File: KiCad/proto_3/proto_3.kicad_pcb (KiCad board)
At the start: 2 copper layers, 129 x 49 mm, 13 parts, among them J1 1729128, J2 1729128

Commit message: removed AC markings on L and N lines on AC input. Added individual L and P symbols to AC input lines. Need to create nets for each.
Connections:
- net Net-(D1-A1) renamed +5V
- C2 pad 2: Net-(D1-A2) -> GND
- C3 pad 2: Net-(D1-A2) -> GND
- C4 pad 2: Net-(D1-A2) -> GND
- CY1 pad 2: Net-(D1-A2) -> GND
- D1 pad 2: Net-(D1-A2) -> GND
- FUSE1 pad 1: Net-(FUSE1-Pad1) -> AC
- J1 pad 2: Net-(D1-A2) -> GND
- J2 pad 1: GND -> AC
- J2 pad 2: Net-(FUSE1-Pad1) -> AC
- U1 pad 2: GND -> AC
- U1 pad 5: Net-(D1-A2) -> GND
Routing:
- net AC: track 0.00 -> 141.5 mm
- net Net-(D1-A2): track 106.1 -> 0.00 mm
- net Net-(FUSE1-Pad1): track 40.0 -> 0.00 mm
- net GND: track 101.6 -> 106.1 mm
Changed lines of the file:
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@@
 	(net 6 "Net-(LDM1-Pad2)")
 	(net 7 "GND")
-	(net 8 "Net-(D1-A2)")
-	(net 9 "Net-(D1-A1)")
-	(net 10 "Net-(FUSE1-Pad1)")
+	(net 8 "+5V")
+	(net 9 "AC")
 	(footprint "Capacitor-470uF-16V:CAP_RHT_8X11P5_NCH"
 		(layer "F.Cu")
@@
 			(layers "*.Cu" "*.Mask")
 			(remove_unused_layers no)
-			(net 8 "Net-(D1-A2)")
+			(net 7 "GND")
 			(pintype "unspecified")
 		)
@@
 			(layers "*.Cu" "*.Mask")
 			(remove_unused_layers no)
-			(net 9 "Net-(D1-A1)")
+			(net 8 "+5V")
 			(pinfunction "1")
 			(pintype "unspecified")
@@
 			(layers "*.Cu" "*.Mask")
 			(remove_unused_layers no)
-			(net 7 "GND")
+			(net 9 "AC")
 			(pinfunction "AC(N)")
 			(pintype "bidirectional")
@@
 			(layers "*.Cu" "*.Mask")
 			(remove_unused_layers no)
-			(net 8 "Net-(D1-A2)")
+			(net 7 "GND")
 			(pinfunction "-Vo")
 			(pintype "bidirectional")
@@
 		)
 		(property "Datasheet" "1729128"
-			(at 0 0 90)
+			(at 0 0 270)
 			(layer "F.Fab")
 			(hide yes)
@@
 		)
 		(property "Description" ""
-			(at 0 0 90)
+			(at 0 0 270)
 			(layer "F.Fab")
 			(hide yes)
@@
 			(layers "*.Cu" "*.Mask")
 			(remove_unused_layers no)
-			(net 9 "Net-(D1-A1)")
+			(net 8 "+5V")
 			(pinfunction "1")
 			(pintype "unspecified")
@@
 			(layers "*.Cu" "*.Mask")
 			(remove_unused_layers no)
-			(net 8 "Net-(D1-A2)")
+			(net 7 "GND")
 			(pinfunction "2")
 			(pintype "unspecified")
@@
 			(layers "*.Cu" "*.Mask")
 			(remove_unused_layers no)
-			(net 9 "Net-(D1-A1)")
+			(net 8 "+5V")
 			(pintype "unspecified")
 		)
@@
 			(layers "*.Cu" "*.Mask")
 			(remove_unused_layers no)
-			(net 8 "Net-(D1-A2)")
+			(net 7 "GND")
 			(pintype "unspecified")
 		)
@@
 		(embedded_fonts no)
 		(model "/home/none/Downloads/AIUR_06_472K/AIUR-06_ABR.step"
-			(hide yes)
 			(offset
 				(xyz 0 0 0)
@@
 			(size 2.1844 2.1844)
 			(layers "F.Cu" "F.Mask" "F.Paste")
-			(net 9 "Net-(D1-A1)")
+			(net 8 "+5V")
 			(pinfunction "A1")
 			(pintype "passive")
@@
 			(size 2.1844 2.1844)
 			(layers "F.Cu" "F.Mask" "F.Paste")
-			(net 8 "Net-(D1-A2)")
+			(net 7 "GND")
 			(pinfunction "A2")
 			(pintype "passive")
@@
 			(layers "*.Cu" "*.Mask")
 			(remove_unused_layers no)
-			(net 8 "Net-(D1-A2)")
+			(net 7 "GND")
 			(pintype "passive")
 			(solder_mask_margin 0.102)
@@
 			(layers "*.Cu" "*.Mask")
 			(remove_unused_layers no)
-			(net 10 "Net-(FUSE1-Pad1)")
+			(net 9 "AC")
 			(pinfunction "1")
 			(pintype "unspecified")
@@
 			(layers "*.Cu" "*.Mask")
 			(remove_unused_layers no)
-			(net 9 "Net-(D1-A1)")
+			(net 8 "+5V")
 			(pintype "unspecified")
 		)
@@
 			(layers "*.Cu" "*.Mask")
 			(remove_unused_layers no)
-			(net 8 "Net-(D1-A2)")
+			(net 7 "GND")
 			(pintype "unspecified")
 		)
@@
 		)
 		(property "Datasheet" "1729128"
-			(at 0 0 90)
+			(at 0 0 270)
 			(layer "F.Fab")
 			(hide yes)
@@
 		)
 		(property "Description" ""
-			(at 0 0 90)
+			(at 0 0 270)
 			(layer "F.Fab")
 			(hide yes)
@@
 			(layers "*.Cu" "*.Mask")
 			(remove_unused_layers no)
-			(net 7 "GND")
+			(net 9 "AC")
 			(pinfunction "1")
 			(pintype "unspecified")
@@
 			(layers "*.Cu" "*.Mask")
 			(remove_unused_layers no)
-			(net 10 "Net-(FUSE1-Pad1)")
+			(net 9 "AC")
 			(pinfunction "2")
 			(pintype "unspecified")
@@
 	)
 	(segment
-		(start 116.5 118.62)
-		(end 202.5 118.62)
-		(width 0.7814)
-		(layer "F.Cu")
-		(net 7)
-	)
-	(segment
-		(start 202.5 118.62)
-		(end 212.7 118.62)
-		(width 0.7814)
-		(layer "F.Cu")
-		(net 7)
-	)
-	(segment
-		(start 212.7 118.62)
-		(end 216.5 122.42)
-		(width 0.7814)
-		(layer "F.Cu")
-		(net 7)
-	)
-	(segment
 		(start 192.5 107.12)
 		(end 206.5 107.12)
 		(width 0.7814)
 		(layer "F.Cu")
-		(net 8)
+		(net 7)
 	)
 	(segment
@@
 		(width 0.7814)
 		(layer "F.Cu")
-		(net 8)
+		(net 7)
 	)
 	(segment
@@
 		(width 0.7814)
 		(layer "F.Cu")
-		(net 8)
+		(net 7)
 	)
 	(segment
@@
 		(width 0.7814)
 		(layer "F.Cu")
-		(net 8)
+		(net 7)
 	)
 	(segment
@@
 		(width 0.7814)
 		(layer "F.Cu")
-		(net 8)
+		(net 7)
 	)
 	(segment
@@
 		(width 0.7814)
 		(layer "F.Cu")
-		(net 8)
+		(net 7)
 	)
 	(segment
@@
 		(width 0.7814)
 		(layer "F.Cu")
-		(net 8)
+		(net 7)
 	)
 	(segment
@@
 		(width 0.7814)
 		(layer "F.Cu")
-		(net 8)
+		(net 7)
 	)
 	(segment
@@
 		(width 0.7814)
 		(layer "F.Cu")
-		(net 8)
+		(net 7)
 	)
 	(segment
@@
 		(width 0.7814)
 		(layer "F.Cu")
-		(net 8)
+		(net 7)
 	)
 	(segment
@@
 		(width 0.7814)
 		(layer "F.Cu")
-		(net 8)
+		(net 7)
 	)
 	(segment
@@
 		(width 0.7814)
 		(layer "F.Cu")
-		(net 8)
+		(net 7)
 	)
 	(segment
@@
 		(width 0.7814)
 		(layer "F.Cu")
-		(net 8)
+		(net 7)
 	)
 	(segment
@@
 		(width 0.7814)
 		(layer "F.Cu")
-		(net 8)
+		(net 7)
 	)
 	(segment
@@
 		(width 0.7814)
 		(layer "F.Cu")
-		(net 8)
+		(net 7)
 	)
 	(segment
@@
 		(width 0.7814)
 		(layer "F.Cu")
-		(net 8)
+		(net 7)
 	)
 	(segment
@@
 		(width 0.7814)
 		(layer "F.Cu")
-		(net 8)
+		(net 7)
 	)
 	(segment
@@
 		(width 0.7814)
 		(layer "F.Cu")
-		(net 9)
+		(net 8)
 	)
 	(segment
@@
 		(width 0.7814)
 		(layer "F.Cu")
-		(net 9)
+		(net 8)
 	)
 	(segment
@@
 		(width 0.7814)
 		(layer "F.Cu")
-		(net 9)
+		(net 8)
 	)
 	(segment
@@
 		(width 0.2)
 		(layer "F.Cu")
-		(net 9)
+		(net 8)
 	)
 	(segment
@@
 		(width 0.2)
 		(layer "F.Cu")
-		(net 9)
+		(net 8)
 	)
 	(segment
@@
 		(width 0.7814)
 		(layer "F.Cu")
-		(net 9)
+		(net 8)
 	)
 	(segment
@@
 		(width 0.7814)
 		(layer "F.Cu")
-		(net 9)
+		(net 8)
 	)
 	(segment
@@
 		(width 0.2)
 		(layer "F.Cu")
-		(net 9)
+		(net 8)
 	)
 	(segment
@@
 		(width 0.7814)
 		(layer "F.Cu")
-		(net 9)
+		(net 8)
 	)
 	(segment
@@
 		(width 0.7814)
 		(layer "F.Cu")
-		(net 9)
+		(net 8)
 	)
 	(segment
@@
 		(width 0.7814)
 		(layer "F.Cu")
+		(net 8)
+	)
+	(segment
+		(start 116.5 118.62)
+		(end 202.5 118.62)
+		(width 0.7814)
+		(layer "F.Cu")
 		(net 9)
 	)
@@
 		(width 0.7814)
 		(layer "F.Cu")
-		(net 10)
+		(net 9)
+	)
+	(segment
+		(start 202.5 118.62)
+		(end 212.7 118.62)
+		(width 0.7814)
+		(layer "F.Cu")
+		(net 9)
+	)
+	(segment
+		(start 212.7 118.62)
+		(end 216.5 122.42)
+		(width 0.7814)
+		(layer "F.Cu")
+		(net 9)
 	)
 	(segment
@@
 		(width 0.7814)
 		(layer "F.Cu")
-		(net 10)
+		(net 9)
 	)
 	(segment
@@
 		(width 0.7814)
 		(layer "F.Cu")
-		(net 10)
+		(net 9)
 	)
 	(zone

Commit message: labeled nets and netclasses for organization
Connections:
- FUSE1 pad 1: AC -> Net-(FUSE1-Pad1)
- J2 pad 1: AC -> Net-(U1-AC(N))
- J2 pad 2: AC -> Net-(FUSE1-Pad1)
- U1 pad 2: AC -> Net-(U1-AC(N))
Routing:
- net AC: track 141.5 -> 0.00 mm
- net Net-(U1-AC(N)): track 0.00 -> 101.6 mm
- net Net-(FUSE1-Pad1): track 0.00 -> 40.0 mm
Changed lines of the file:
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@@
 	(net 7 "GND")
 	(net 8 "+5V")
-	(net 9 "AC")
+	(net 9 "Net-(U1-AC(N))")
+	(net 10 "Net-(FUSE1-Pad1)")
 	(footprint "Capacitor-470uF-16V:CAP_RHT_8X11P5_NCH"
 		(layer "F.Cu")
@@
 			(layers "*.Cu" "*.Mask")
 			(remove_unused_layers no)
-			(net 9 "AC")
+			(net 9 "Net-(U1-AC(N))")
 			(pinfunction "AC(N)")
 			(pintype "bidirectional")
@@
 			(layers "*.Cu" "*.Mask")
 			(remove_unused_layers no)
-			(net 9 "AC")
+			(net 10 "Net-(FUSE1-Pad1)")
 			(pinfunction "1")
 			(pintype "unspecified")
@@
 			(layers "*.Cu" "*.Mask")
 			(remove_unused_layers no)
-			(net 9 "AC")
+			(net 9 "Net-(U1-AC(N))")
 			(pinfunction "1")
 			(pintype "unspecified")
@@
 			(layers "*.Cu" "*.Mask")
 			(remove_unused_layers no)
-			(net 9 "AC")
+			(net 10 "Net-(FUSE1-Pad1)")
 			(pinfunction "2")
 			(pintype "unspecified")
@@
 	)
 	(segment
-		(start 199.62 126.5)
-		(end 215.5 126.5)
-		(width 0.7814)
-		(layer "F.Cu")
-		(net 9)
-	)
-	(segment
 		(start 202.5 118.62)
 		(end 212.7 118.62)
@@
 	)
 	(segment
+		(start 199.62 126.5)
+		(end 215.5 126.5)
+		(width 0.7814)
+		(layer "F.Cu")
+		(net 10)
+	)
+	(segment
 		(start 175.58 126.62)
 		(end 199.5 126.62)
 		(width 0.7814)
 		(layer "F.Cu")
-		(net 9)
+		(net 10)
 	)
 	(segment
@@
 		(width 0.7814)
 		(layer "F.Cu")
-		(net 9)
+		(net 10)
 	)
 	(zone

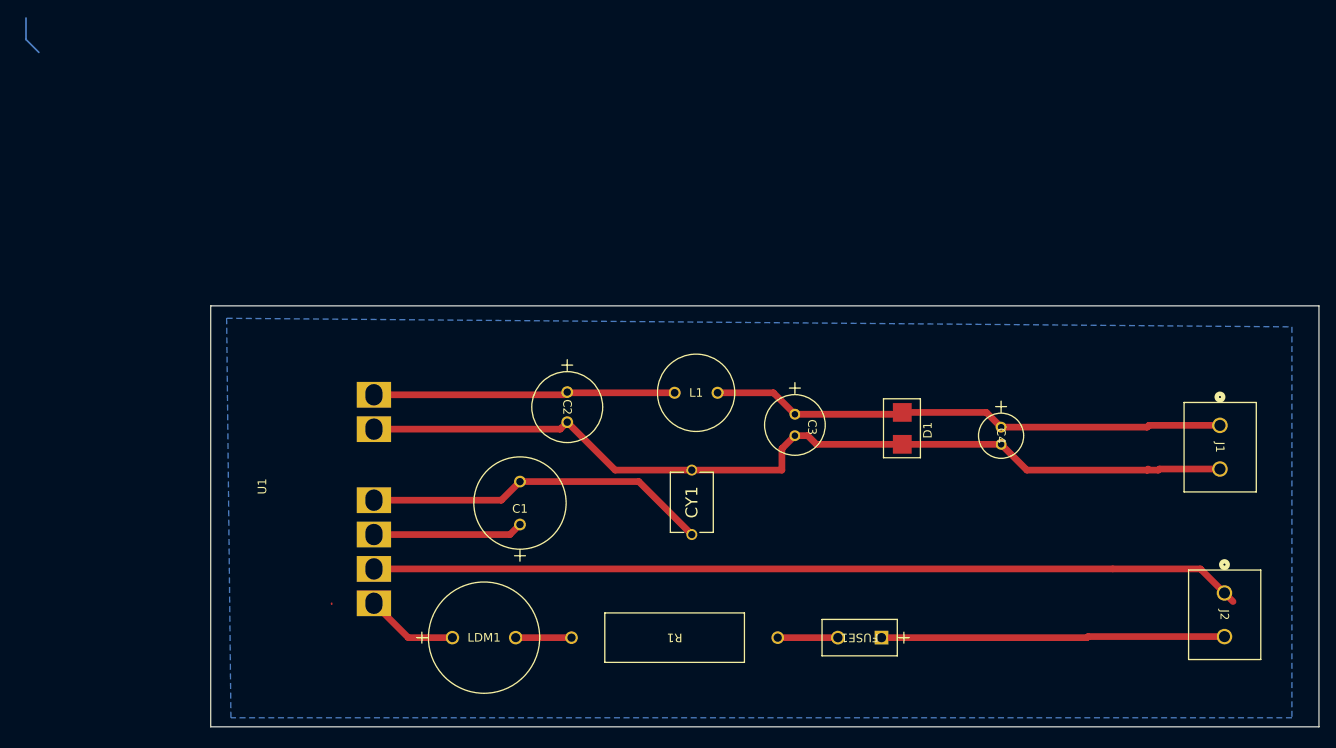
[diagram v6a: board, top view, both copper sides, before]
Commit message: re-added ground plane
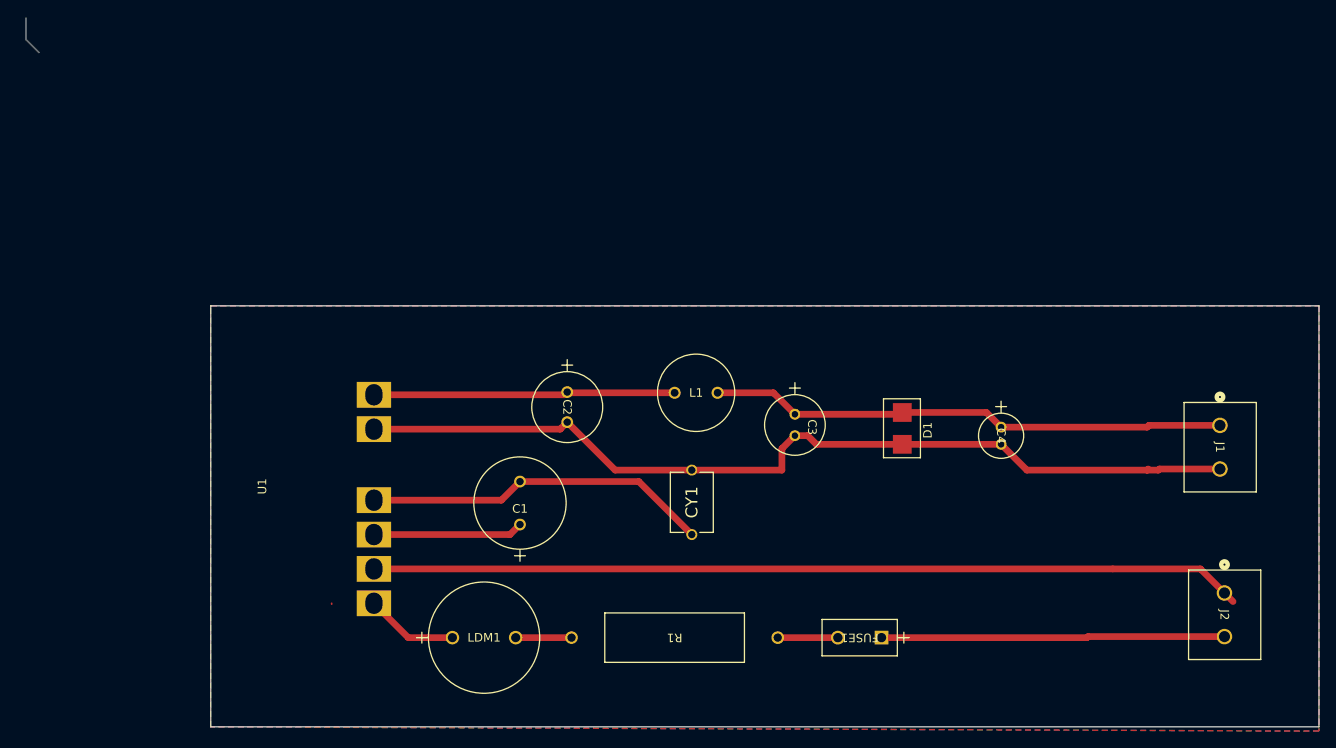
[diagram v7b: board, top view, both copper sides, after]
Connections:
- net +5V renamed /DC_OUT
- net Net-(FUSE1-Pad1) renamed /AC_IN_PHASE
- net Net-(FUSE1-Pad2) renamed /AC_FUSE
- net Net-(LDM1-Pad2) renamed /AC_FILTER_IN
- net Net-(U1-+V(cap)) renamed /ACDC_VCAP_POS
- net Net-(U1-+Vo) renamed /DC_OUT_UNFILTERED
- net Net-(U1--V(cap)) renamed /ACDC_VCAP_NEG
- net Net-(U1-AC(L)) renamed /AC_FILTER_OUT
- net Net-(U1-AC(N)) renamed /AC_IN_NEUTRAL
- C2 pad 2: GND -> /GND
- C3 pad 2: GND -> unconnected-(C3-Pad2)
- C4 pad 2: GND -> /GND
- CY1 pad 2: GND -> /GND
- D1 pad 2: GND -> /GND
- J1 pad 2: GND -> /GND
- U1 pad 5: GND -> /GND
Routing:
- added copper zone on B.Cu, net /GND
- added copper zone on F.Cu, net /GND
- removed copper zone on B.Cu, net GND

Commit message: moved traces around, added ground pour again
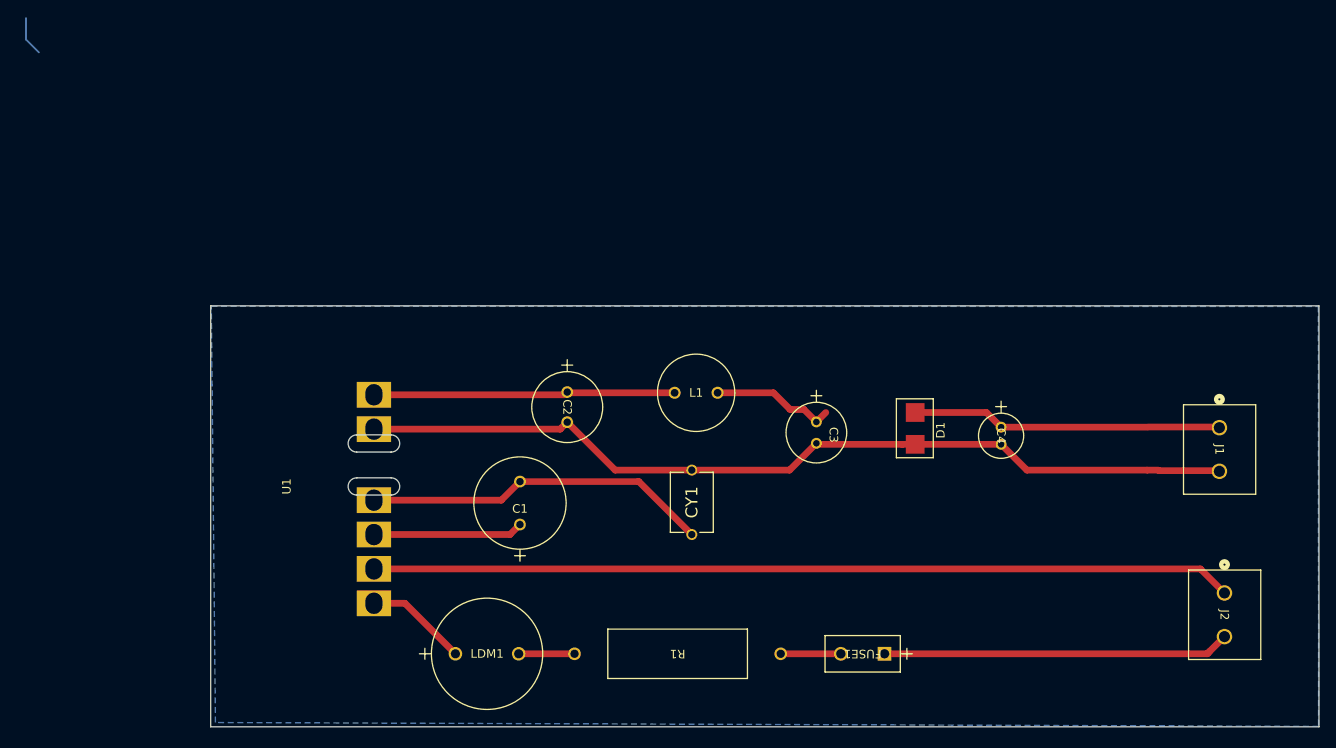
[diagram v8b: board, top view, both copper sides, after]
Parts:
- U1: footprint stuff:transformer_MPL-05SC-F -> stuff:transformer_MPL-05SC-F_new
- moved C3 2.65 mm to (168.0, 101.5)
- moved FUSE1 1.91 mm to (175.9, 128.5)
- moved LDM1 1.91 mm to (126.0, 128.5)
- moved R1 1.91 mm to (163.8, 128.5)
- moved D1 1.50 mm to (179.5, 102.5)
- moved J1 0.27 mm to (214.9, 102.2)
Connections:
- C3 pad 2: unconnected-(C3-Pad2) -> /GND
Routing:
- net GND: track 106.1 -> 0.00 mm
- net /GND: track 0.00 -> 103.5 mm
- net /DC_OUT: track 61.1 -> 52.2 mm
- net /AC_IN_NEUTRAL: track 101.6 -> 100.2 mm
- net /AC_FILTER_OUT: track 10.8 -> 11.9 mm
- net /AC_IN_PHASE: track 40.0 -> 40.8 mm
- removed copper zone on F.Cu, net /GND
